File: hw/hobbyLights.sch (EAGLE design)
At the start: 68 parts, among them Q1 PMV22EN, U1 MCP73831-2, U2 POWER, U3 BD48K28G, U4 ATMEGA32U4-AU, U5 TPS61222, Y1 RESONATORSMD

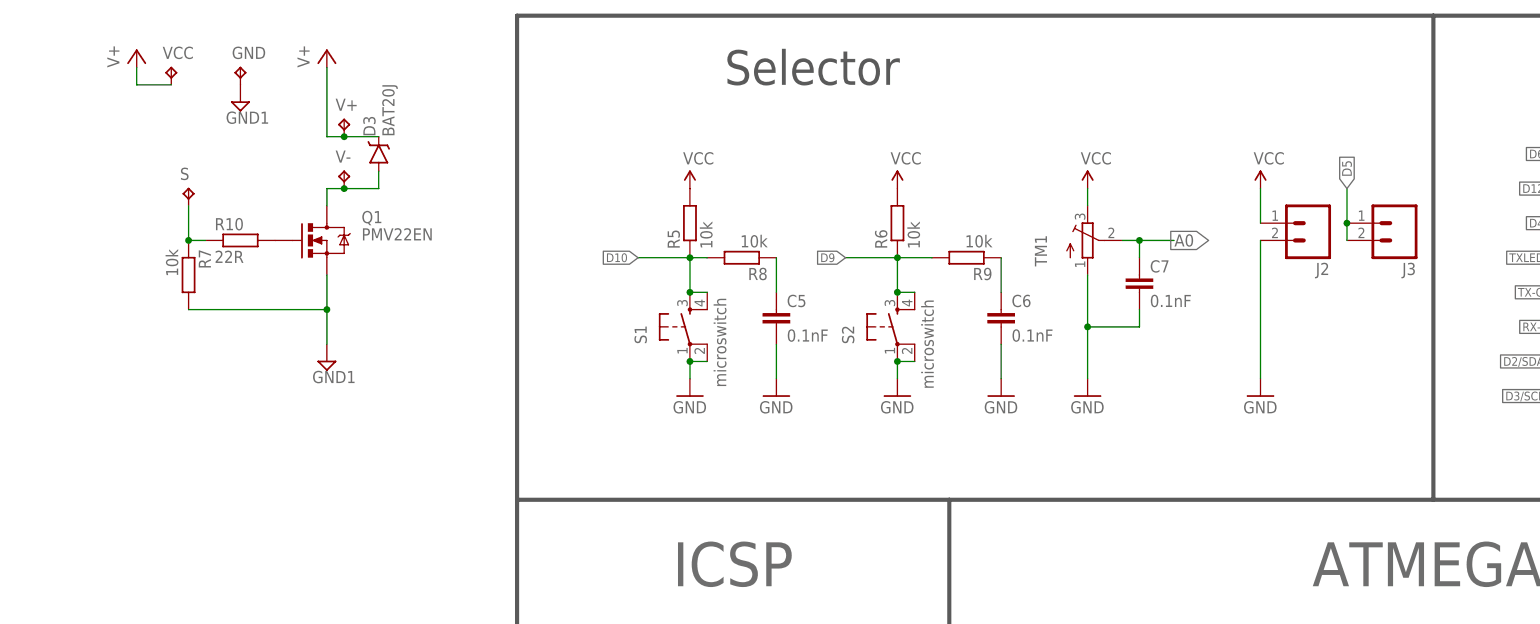
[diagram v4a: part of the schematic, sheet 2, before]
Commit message: Minor updates and silk screen improvements.
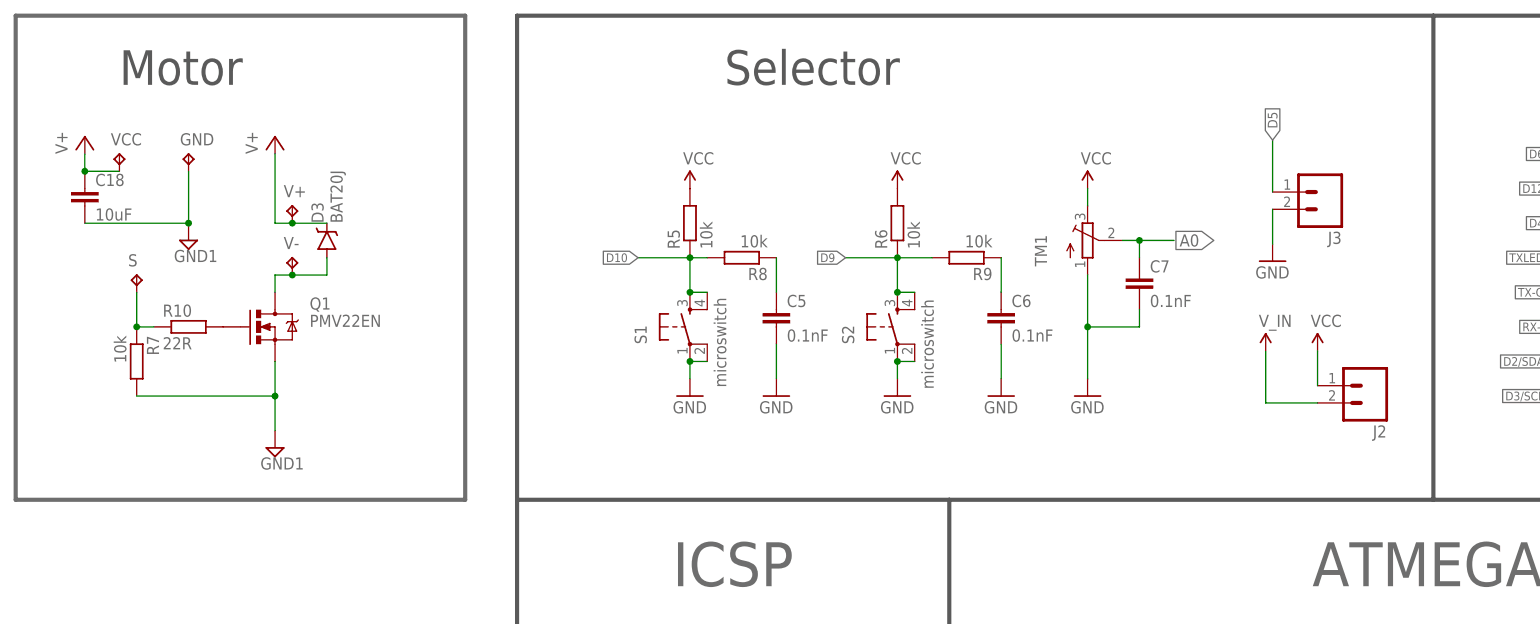
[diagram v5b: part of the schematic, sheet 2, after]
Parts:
- added C18: 10uF, rcl:C-EUC0805
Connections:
- net D5: no longer J3.2
- net GND: now also J3.2; no longer J2.2
- net GND1: now also C18.2
- net V+: now also C18.1
- net V_BATT: now also J2.2
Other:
- note added: "Motor"
- moved on the sheet: D3, GND, J2, J3, Q1, R10, R7, S, V+, V-, VCC
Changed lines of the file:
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@@
 <part name="SUPPLY8" library="supply2" deviceset="GND1" device=""/>
 <part name="SUPPLY9" library="supply2" deviceset="GND1" device=""/>
+<part name="SUPPLY10" library="SparkFun-Aesthetics" deviceset="V_BATT" device="" value="V_IN"/>
+<part name="C18" library="rcl" deviceset="C-EU" device="C0805" value="10uF"/>
 </parts>
 <sheets>
@@
 <text x="314.96" y="27.94" size="3.81" layer="97" ratio="12">MCU Interface</text>
 <text x="157.48" y="7.62" size="3.81" layer="95" font="fixed">copyright by F. Malpartida</text>
+<wire x1="5.08" y1="251.46" x2="71.12" y2="251.46" width="0.6096" layer="95"/>
+<wire x1="71.12" y1="251.46" x2="71.12" y2="180.34" width="0.6096" layer="95"/>
+<wire x1="71.12" y1="180.34" x2="5.08" y2="180.34" width="0.6096" layer="95"/>
+<wire x1="5.08" y1="180.34" x2="5.08" y2="251.46" width="0.6096" layer="95"/>
+<text x="20.32" y="241.3" size="5.08" layer="97" ratio="12">Motor</text>
 </plain>
 <instances>
@@
 <instance part="C7" gate="G$1" x="170.18" y="213.36"/>
 <instance part="U$25" gate="G$1" x="281.94" y="101.6"/>
-<instance part="J2" gate="G$1" x="195.58" y="220.98" rot="R180"/>
-<instance part="P+5" gate="1" x="187.96" y="226.06"/>
-<instance part="GND13" gate="1" x="187.96" y="195.58"/>
-<instance part="J3" gate="G$1" x="208.28" y="220.98" rot="R180"/>
+<instance part="J2" gate="G$1" x="203.962" y="197.104" rot="R180"/>
+<instance part="P+5" gate="1" x="196.342" y="202.184"/>
+<instance part="GND13" gate="1" x="189.738" y="215.392"/>
+<instance part="J3" gate="G$1" x="197.358" y="225.552" rot="R180"/>
 <instance part="U$6" gate="G$1" x="281.94" y="109.22"/>
-<instance part="Q1" gate="G$1" x="50.8" y="218.44"/>
-<instance part="R7" gate="G$1" x="30.48" y="213.36" rot="R270"/>
-<instance part="R10" gate="G$1" x="38.1" y="218.44"/>
-<instance part="V+" gate="G$1" x="53.34" y="236.22"/>
-<instance part="V-" gate="G$1" x="53.34" y="228.6"/>
-<instance part="S" gate="G$1" x="30.48" y="226.06"/>
-<instance part="VCC" gate="G$1" x="27.94" y="243.84"/>
-<instance part="GND" gate="G$1" x="38.1" y="243.84"/>
-<instance part="D3" gate="G$1" x="58.42" y="231.14" rot="R90"/>
-<instance part="P+12" gate="VCC" x="22.86" y="246.38"/>
-<instance part="P+13" gate="VCC" x="50.8" y="246.38"/>
-<instance part="SUPPLY8" gate="G$1" x="38.1" y="238.76"/>
-<instance part="SUPPLY9" gate="G$1" x="50.8" y="200.66"/>
+<instance part="Q1" gate="G$1" x="43.18" y="205.74"/>
+<instance part="R7" gate="G$1" x="22.86" y="200.66" rot="R270"/>
+<instance part="R10" gate="G$1" x="30.48" y="205.74"/>
+<instance part="V+" gate="G$1" x="45.72" y="223.52"/>
+<instance part="V-" gate="G$1" x="45.72" y="215.9"/>
+<instance part="S" gate="G$1" x="22.86" y="213.36"/>
+<instance part="VCC" gate="G$1" x="20.32" y="231.14"/>
+<instance part="GND" gate="G$1" x="30.48" y="231.14"/>
+<instance part="D3" gate="G$1" x="50.8" y="218.44" rot="R90"/>
+<instance part="P+12" gate="VCC" x="15.24" y="233.68"/>
+<instance part="P+13" gate="VCC" x="43.18" y="233.68"/>
+<instance part="SUPPLY8" gate="G$1" x="30.48" y="218.44"/>
+<instance part="SUPPLY9" gate="G$1" x="43.18" y="187.96"/>
+<instance part="SUPPLY10" gate="G$1" x="188.722" y="202.184"/>
+<instance part="C18" gate="G$1" x="15.24" y="226.06"/>
 </instances>
 <busses>
@@
 </segment>
 <segment>
+<pinref part="J3" gate="G$1" pin="2"/>
 <pinref part="GND13" gate="1" pin="GND"/>
-<pinref part="J2" gate="G$1" pin="2"/>
-<wire x1="187.96" y1="198.12" x2="187.96" y2="218.44" width="0.1524" layer="91"/>
+<wire x1="189.738" y1="223.012" x2="189.738" y2="217.932" width="0.1524" layer="91"/>
 </segment>
 </net>
@@
 <pinref part="P+5" gate="1" pin="VCC"/>
 <pinref part="J2" gate="G$1" pin="1"/>
-<wire x1="187.96" y1="226.06" x2="187.96" y2="220.98" width="0.1524" layer="91"/>
+<wire x1="196.342" y1="202.184" x2="196.342" y2="197.104" width="0.1524" layer="91"/>
 </segment>
 </net>
@@
 <segment>
 <pinref part="J3" gate="G$1" pin="1"/>
-<wire x1="200.66" y1="220.98" x2="200.66" y2="226.06" width="0.1524" layer="91"/>
-<label x="200.66" y="226.06" size="1.4224" layer="95" font="fixed" rot="R90" xref="yes"/>
-<pinref part="J3" gate="G$1" pin="2"/>
-<wire x1="200.66" y1="218.44" x2="200.66" y2="220.98" width="0.1524" layer="91"/>
-<junction x="200.66" y="220.98"/>
+<wire x1="189.738" y1="225.552" x2="189.738" y2="233.172" width="0.1524" layer="91"/>
+<label x="189.738" y="233.172" size="1.4224" layer="95" font="fixed" rot="R90" xref="yes"/>
 </segment>
 </net>
@@
 <pinref part="TM1" gate="G$1" pin="S"/>
 <wire x1="175.26" y1="218.44" x2="170.18" y2="218.44" width="0.1524" layer="91"/>
-<label x="180.34" y="218.44" size="1.778" layer="95" rot="R180" xref="yes"/>
+<label x="181.102" y="218.44" size="1.778" layer="95" rot="R180" xref="yes"/>
 <pinref part="C7" gate="G$1" pin="1"/>
 <wire x1="170.18" y1="218.44" x2="167.64" y2="218.44" width="0.1524" layer="91"/>
@@
 <pinref part="R7" gate="G$1" pin="1"/>
 <pinref part="R10" gate="G$1" pin="1"/>
-<wire x1="30.48" y1="218.44" x2="33.02" y2="218.44" width="0.1524" layer="91"/>
-<wire x1="30.48" y1="218.44" x2="30.48" y2="223.52" width="0.1524" layer="91"/>
-<junction x="30.48" y="218.44"/>
+<wire x1="22.86" y1="205.74" x2="25.4" y2="205.74" width="0.1524" layer="91"/>
+<wire x1="22.86" y1="205.74" x2="22.86" y2="210.82" width="0.1524" layer="91"/>
+<junction x="22.86" y="205.74"/>
 <pinref part="S" gate="G$1" pin="TP"/>
 </segment>
@@
 <segment>
 <pinref part="Q1" gate="G$1" pin="D"/>
-<wire x1="50.8" y1="226.06" x2="50.8" y2="223.52" width="0.1524" layer="91"/>
+<wire x1="43.18" y1="213.36" x2="43.18" y2="210.82" width="0.1524" layer="91"/>
 <pinref part="V-" gate="G$1" pin="TP"/>
-<wire x1="50.8" y1="226.06" x2="53.34" y2="226.06" width="0.1524" layer="91"/>
+<wire x1="43.18" y1="213.36" x2="45.72" y2="213.36" width="0.1524" layer="91"/>
 <pinref part="D3" gate="G$1" pin="A"/>
-<wire x1="53.34" y1="226.06" x2="58.42" y2="226.06" width="0.1524" layer="91"/>
-<wire x1="58.42" y1="226.06" x2="58.42" y2="228.6" width="0.1524" layer="91"/>
-<junction x="53.34" y="226.06"/>
+<wire x1="45.72" y1="213.36" x2="50.8" y2="213.36" width="0.1524" layer="91"/>
+<wire x1="50.8" y1="213.36" x2="50.8" y2="215.9" width="0.1524" layer="91"/>
+<junction x="45.72" y="213.36"/>
 </segment>
 </net>
@@
 <pinref part="GND" gate="G$1" pin="TP"/>
 <pinref part="SUPPLY8" gate="G$1" pin="GND1"/>
+<wire x1="30.48" y1="220.98" x2="30.48" y2="228.6" width="0.1524" layer="91"/>
+<pinref part="C18" gate="G$1" pin="2"/>
+<wire x1="15.24" y1="220.98" x2="30.48" y2="220.98" width="0.1524" layer="91"/>
+<junction x="30.48" y="220.98"/>
 </segment>
 <segment>
 <pinref part="Q1" gate="G$1" pin="S"/>
-<wire x1="50.8" y1="203.2" x2="50.8" y2="208.28" width="0.1524" layer="91"/>
+<wire x1="43.18" y1="190.5" x2="43.18" y2="195.58" width="0.1524" layer="91"/>
 <pinref part="R7" gate="G$1" pin="2"/>
-<wire x1="50.8" y1="208.28" x2="50.8" y2="213.36" width="0.1524" layer="91"/>
-<wire x1="30.48" y1="208.28" x2="50.8" y2="208.28" width="0.1524" layer="91"/>
-<junction x="50.8" y="208.28"/>
+<wire x1="43.18" y1="195.58" x2="43.18" y2="200.66" width="0.1524" layer="91"/>
+<wire x1="22.86" y1="195.58" x2="43.18" y2="195.58" width="0.1524" layer="91"/>
+<junction x="43.18" y="195.58"/>
 <pinref part="SUPPLY9" gate="G$1" pin="GND1"/>
 </segment>
@@
 <segment>
 <pinref part="P+12" gate="VCC" pin="VCC"/>
-<wire x1="22.86" y1="243.84" x2="22.86" y2="241.3" width="0.1524" layer="91"/>
+<wire x1="15.24" y1="231.14" x2="15.24" y2="228.6" width="0.1524" layer="91"/>
 <pinref part="VCC" gate="G$1" pin="TP"/>
-<wire x1="22.86" y1="241.3" x2="27.94" y2="241.3" width="0.1524" layer="91"/>
+<wire x1="15.24" y1="228.6" x2="20.32" y2="228.6" width="0.1524" layer="91"/>
+<pinref part="C18" gate="G$1" pin="1"/>
+<junction x="15.24" y="228.6"/>
 </segment>
 <segment>
 <pinref part="V+" gate="G$1" pin="TP"/>
-<wire x1="50.8" y1="233.68" x2="50.8" y2="243.84" width="0.1524" layer="91"/>
-<wire x1="53.34" y1="233.68" x2="50.8" y2="233.68" width="0.1524" layer="91"/>
+<wire x1="43.18" y1="220.98" x2="43.18" y2="231.14" width="0.1524" layer="91"/>
+<wire x1="45.72" y1="220.98" x2="43.18" y2="220.98" width="0.1524" layer="91"/>
 <pinref part="D3" gate="G$1" pin="C"/>
-<wire x1="53.34" y1="233.68" x2="58.42" y2="233.68" width="0.1524" layer="91"/>
-<junction x="53.34" y="233.68"/>
+<wire x1="45.72" y1="220.98" x2="50.8" y2="220.98" width="0.1524" layer="91"/>
+<junction x="45.72" y="220.98"/>
 <pinref part="P+13" gate="VCC" pin="VCC"/>
 </segment>
 </net>
+<net name="V_BATT" class="1">
+<segment>
+<pinref part="J2" gate="G$1" pin="2"/>
+<pinref part="SUPPLY10" gate="G$1" pin="V_BATT"/>
+<wire x1="196.342" y1="194.564" x2="188.722" y2="194.564" width="0.1524" layer="91"/>
+<wire x1="188.722" y1="194.564" x2="188.722" y2="202.184" width="0.1524" layer="91"/>
+</segment>
+</net>
